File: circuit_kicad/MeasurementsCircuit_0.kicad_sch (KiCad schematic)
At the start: 29 parts, among them SW1 SW_DPST_x2

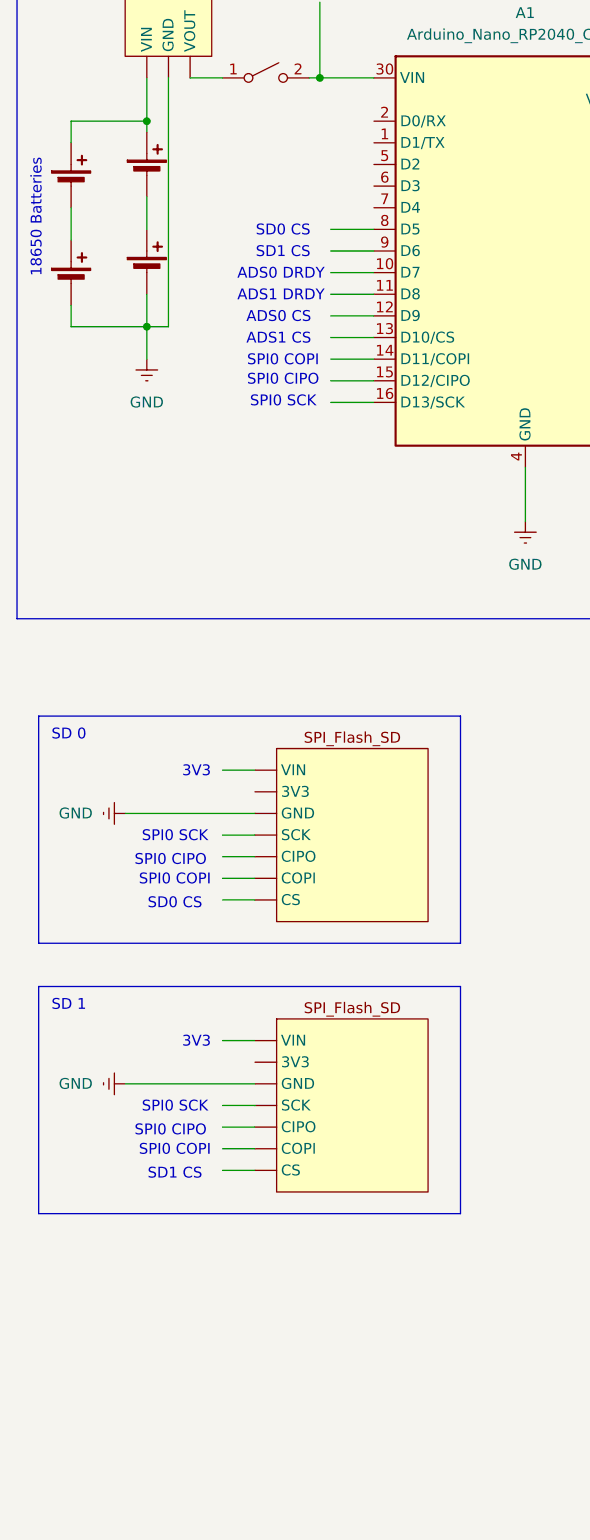
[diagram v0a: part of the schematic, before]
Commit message: Add buzzer to kicad
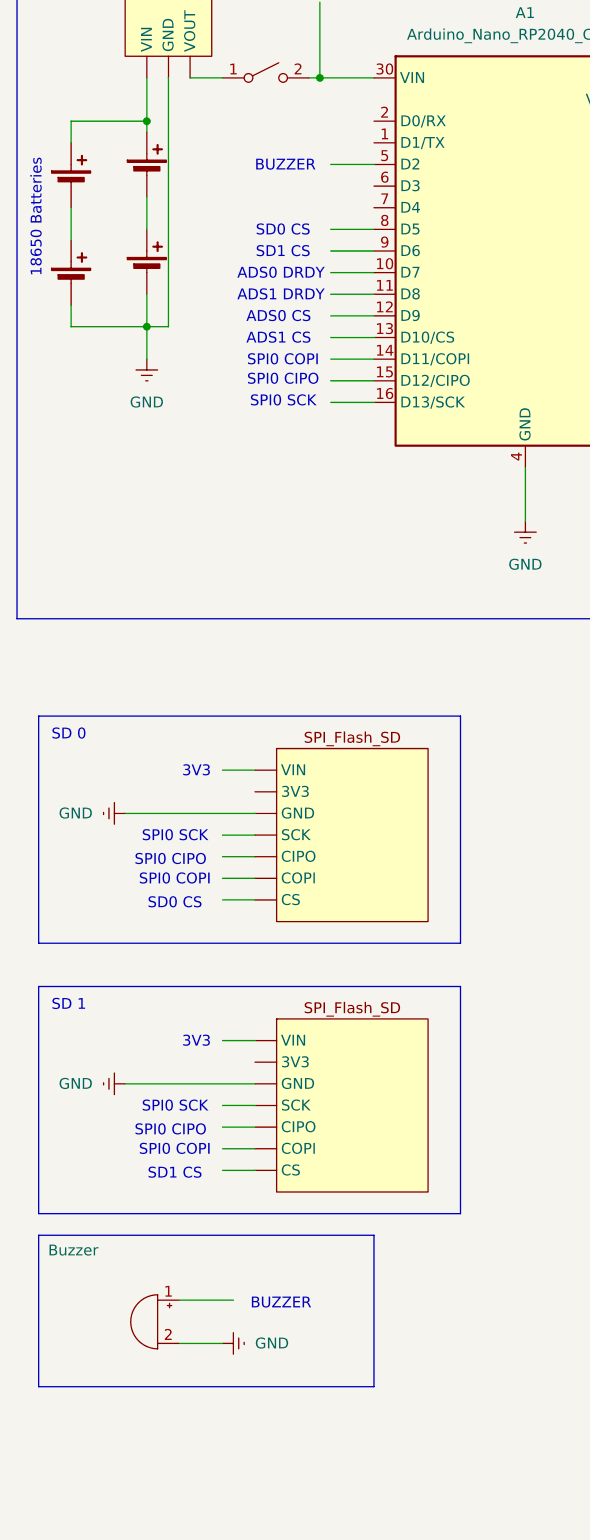
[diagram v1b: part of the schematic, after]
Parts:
- added BZ1: Buzzer, symbol Device:Buzzer
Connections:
- net GND: now also BZ1.2 (-)
- new net: C2. (AIN7), S1. (OUT)
- new net: C2. (AIN7), S6. (OUT)
- new net: C2. (AIN7), L2. (HV4)
- new net: C2. (AIN7), S4. (OUT)
- new net: C2. (AIN7), S2. (OUT)
- new net: C2. (AIN7), L1. (HV4) (x4)
- new net: C2. (AIN7), S3. (OUT)
- new net: C2. (AIN7), S5. (OUT)
- new net: C3. (AIN7), S11. (OUT)
- new net: C3. (AIN7), L5. (HV4)
- new net: C3. (AIN7), S10. (OUT)
- new net: C3. (AIN7), S12. (OUT)
- new net: C3. (AIN7), L4. (HV4) (x4)
- new net: C3. (AIN7), S13. (OUT)
- new net: C3. (AIN7), S8. (OUT)
- new net: C3. (AIN7), S7. (OUT)
- new net: C3. (AIN7), S14. (OUT)
- new net: C3. (AIN7), S9. (OUT)
- new net: S10. (OUT), S11. (OUT), S12. (OUT), S13. (OUT), S14. (OUT), S7. (OUT), S8. (OUT), S9. (OUT)
- new net: S1. (OUT), S2. (OUT), S3. (OUT), S4. (OUT), S5. (OUT), S6. (OUT)
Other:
- note added: "BUZZER"
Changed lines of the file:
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@@
 	(paper "A3")
 	(rectangle
+		(start 26.67 187.96)
+		(end 66.04 205.74)
+		(stroke
+			(width 0)
+			(type default)
+		)
+		(fill
+			(type none)
+		)
+	)
+	(rectangle
 		(start 26.67 127)
 		(end 76.2 153.67)
@@
 		)
 	)
+	(text "BUZZER\n"
+		(exclude_from_sim no)
+		(at 55.118 196.088 0)
+		(effects
+			(font
+				(size 1.27 1.27)
+			)
+		)
+	)
 	(text "5V"
 		(exclude_from_sim no)
@@
 		)
 	)
+	(text "BUZZER\n"
+		(exclude_from_sim no)
+		(at 55.626 62.484 0)
+		(effects
+			(font
+				(size 1.27 1.27)
+			)
+		)
+	)
 	(text "5V"
 		(exclude_from_sim no)
@@
 	(wire
 		(pts
+			(xy 60.96 62.23) (xy 66.04 62.23)
+		)
+		(stroke
+			(width 0)
+			(type default)
+		)
+	)
+	(wire
+		(pts
 			(xy 60.96 74.93) (xy 66.04 74.93)
 		)
@@
 	(wire
 		(pts
+			(xy 43.18 200.66) (xy 48.26 200.66)
+		)
+		(stroke
+			(width 0)
+			(type default)
+		)
+	)
+	(wire
+		(pts
 			(xy 241.3 55.88) (xy 241.3 46.99)
 		)
@@
 	(wire
 		(pts
+			(xy 43.18 195.58) (xy 49.53 195.58)
+		)
+		(stroke
+			(width 0)
+			(type default)
+		)
+	)
+	(wire
+		(pts
 			(xy 213.36 190.5) (xy 223.52 190.5)
 		)
@@
 	)
 	(symbol
+		(lib_id "power:Earth")
+		(at 48.26 200.66 90)
+		(mirror x)
+		(unit 1)
+		(exclude_from_sim no)
+		(in_bom yes)
+		(on_board yes)
+		(dnp no)
+		(property "Reference" "#PWR012"
+			(at 54.61 200.66 0)
+			(effects
+				(font
+					(size 1.27 1.27)
+				)
+				(hide yes)
+			)
+		)
+		(property "Value" "GND"
+			(at 52.07 200.6599 90)
+			(effects
+				(font
+					(size 1.27 1.27)
+				)
+				(justify right)
+			)
+		)
+		(property "Footprint" ""
+			(at 48.26 200.66 0)
+			(effects
+				(font
+					(size 1.27 1.27)
+				)
+				(hide yes)
+			)
+		)
+		(property "Datasheet" "~"
+			(at 48.26 200.66 0)
+			(effects
+				(font
+					(size 1.27 1.27)
+				)
+				(hide yes)
+			)
+		)
+		(property "Description" "Power symbol creates a global label with name \"Earth\""
+			(at 48.26 200.66 0)
+			(effects
+				(font
+					(size 1.27 1.27)
+				)
+				(hide yes)
+			)
+		)
+		(pin "1"
+		)
+		(instances
+			(project "MeasurementsCircuit_0"
+				(path "/645b4507-ed95-4c75-9125-7b8b4069ec23"
+					(reference "#PWR012")
+					(unit 1)
+				)
+			)
+		)
+	)
+	(symbol
 		(lib_name "StrainGaugeModule_3")
 		(lib_id "MeasurementsLibrary:StrainGaugeModule")
@@
 					(unit 1)
 				)
+			)
+		)
+	)
+	(symbol
+		(lib_id "Device:Buzzer")
+		(at 40.64 198.12 0)
+		(mirror y)
+		(unit 1)
+		(exclude_from_sim no)
+		(in_bom yes)
+		(on_board yes)
+		(dnp no)
+		(property "Reference" "BZ1"
+			(at 39.8849 190.5 0)
+			(effects
+				(font
+					(size 1.27 1.27)
+				)
+				(hide yes)
+			)
+		)
+		(property "Value" "Buzzer"
+			(at 30.734 189.738 0)
+			(effects
+				(font
+					(size 1.27 1.27)
+				)
+			)
+		)
+		(property "Footprint" ""
+			(at 41.275 195.58 90)
+			(effects
+				(font
+					(size 1.27 1.27)
+				)
+				(hide yes)
+			)
+		)
+		(property "Datasheet" "~"
+			(at 41.275 195.58 90)
+			(effects
+				(font
+					(size 1.27 1.27)
+				)
+				(hide yes)
+			)
+		)
+		(property "Description" "Buzzer, polarized"
+			(at 40.64 198.12 0)
+			(effects
+				(font
+					(size 1.27 1.27)
+				)
+				(hide yes)
+			)
+		)
+		(pin "1"
+		)
+		(pin "2"
+		)
+		(instances
+			(project ""
+				(path "/645b4507-ed95-4c75-9125-7b8b4069ec23"
+					(reference "BZ1")
+					(unit 1)
+				)
